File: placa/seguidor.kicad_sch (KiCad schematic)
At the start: 19 parts, among them J1 conn_motor, J2 conn_sensores, J3 conn_motor_izq, J4 conn_motor_der, J6 conn_bat, SW2 btn_arranque, U1 ATmega328P-P, U2 LM7805_TO220, Y1 Crystal

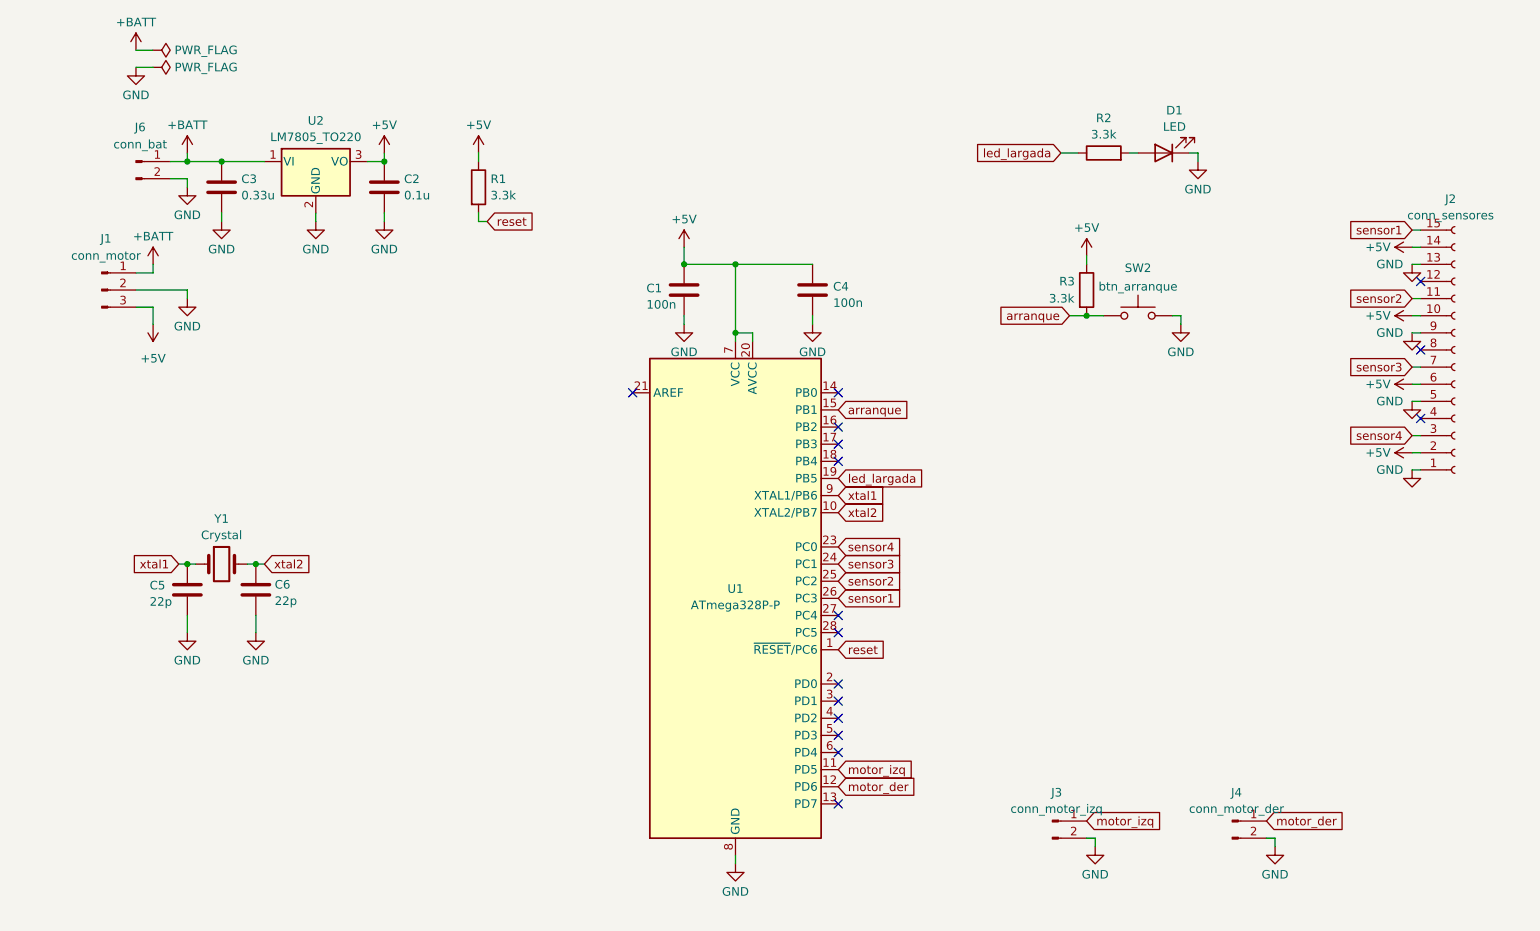
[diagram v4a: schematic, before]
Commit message: placa editada
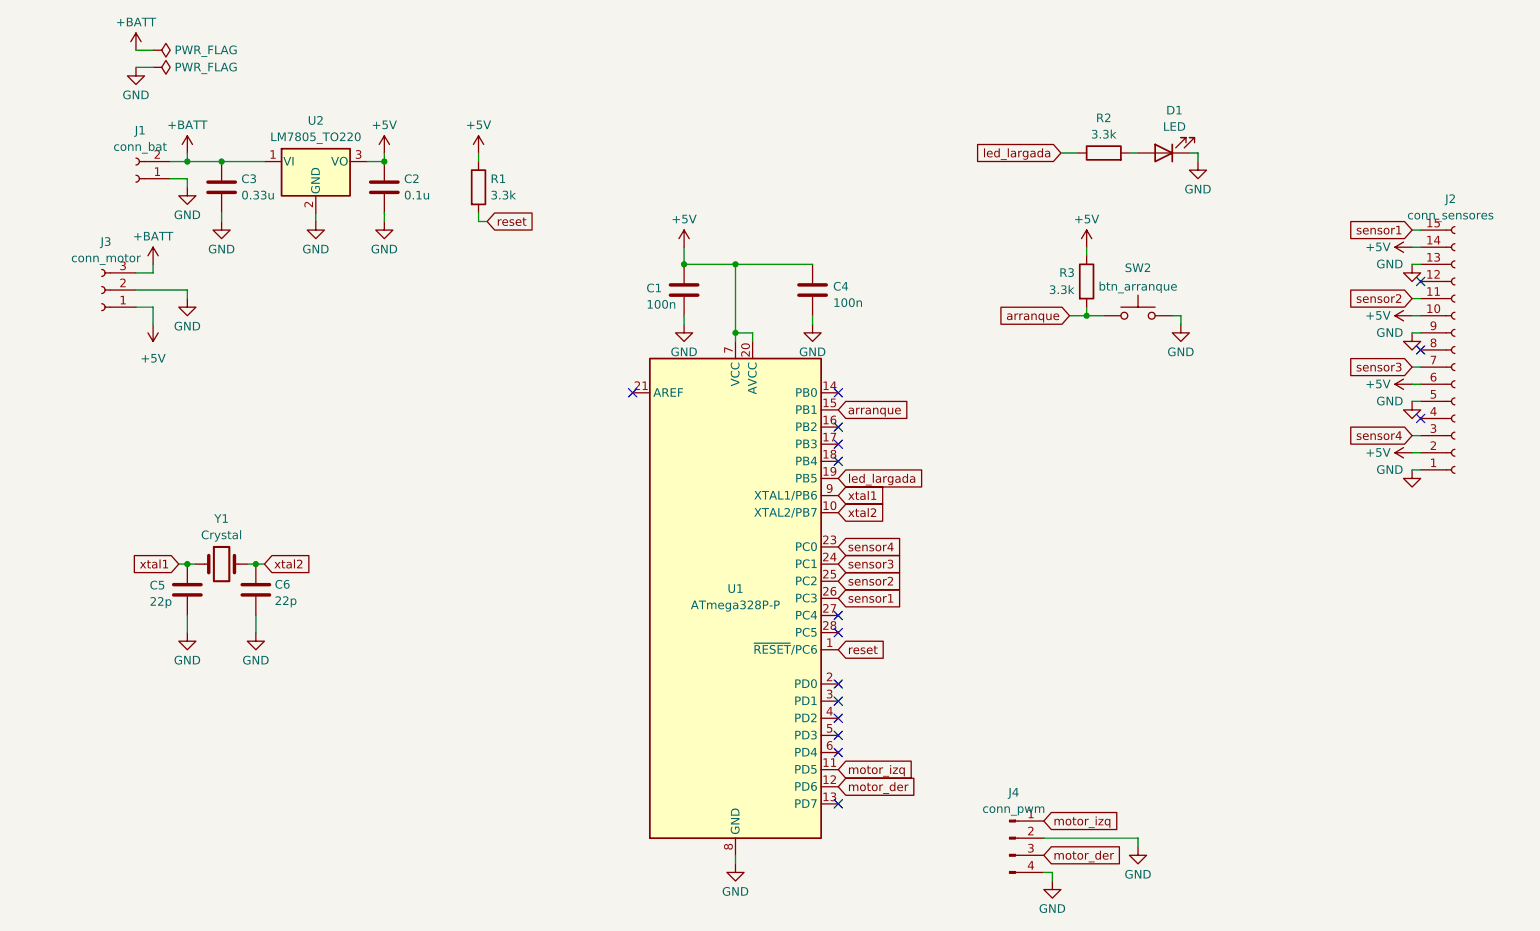
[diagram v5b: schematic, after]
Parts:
- removed J1: conn_motor, symbol Connector:Conn_01x03_Pin
- removed J3: conn_motor_izq, symbol Connector:Conn_01x02_Pin
- removed J4: conn_motor_der, symbol Connector:Conn_01x02_Pin
- removed J6: conn_bat, symbol Connector:Conn_01x02_Pin
- added J1: conn_bat, Connector_Molex:Molex_KK-396_A-41791-0002_1x02_P3.96mm_Vertical, symbol Connector:Conn_01x02_Socket
- added J3: conn_motor, Connector_Molex:Molex_KK-254_AE-6410-03A_1x03_P2.54mm_Vertical, symbol Connector:Conn_01x03_Socket
- added J4: conn_pwm, Connector_PinHeader_2.54mm:PinHeader_1x04_P2.54mm_Vertical, symbol Connector:Conn_01x04_Pin
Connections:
- net +5V: now also J3.1 (Pin_1)
- net +BATT: now also J1.2 (Pin_2), J3.3 (Pin_3)
- net GND: now also J1.1 (Pin_1), J3.2 (Pin_2), J4.2 (Pin_2), J4.4 (Pin_4)
- net motor_der: now also J4.3 (Pin_3)
- net motor_izq: now also J4.1 (Pin_1)
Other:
- moved on the sheet: R3
